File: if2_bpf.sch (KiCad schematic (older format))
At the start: 16 parts

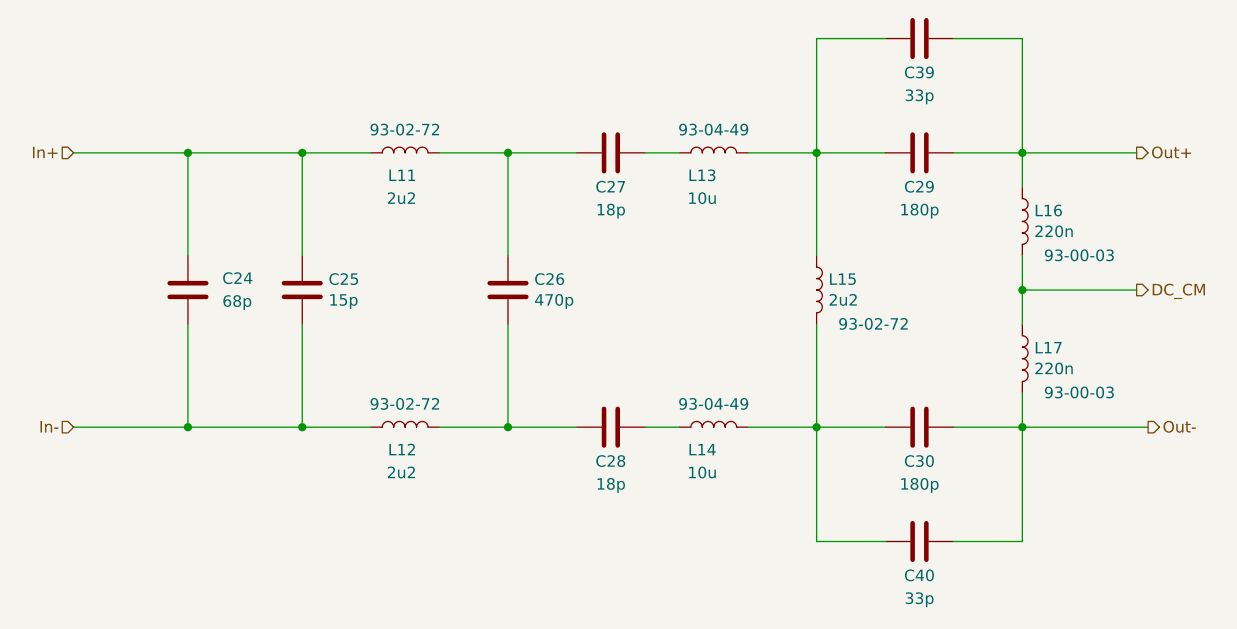
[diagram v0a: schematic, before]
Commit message: FPGA change and new project file
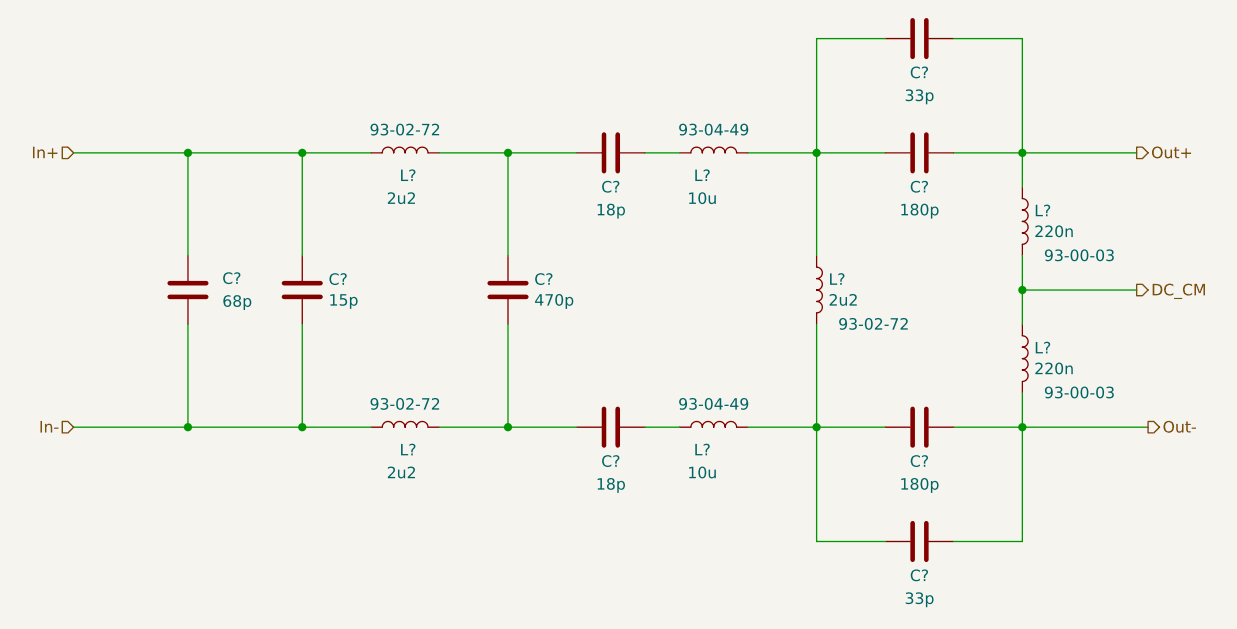
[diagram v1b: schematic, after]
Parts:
- renumbered C24 to C?, C25 to C?, C27 to C?, C29 to C?, C30 to C?, C28 to C?, C26 to C?, C39 to C?, C40 to C?, L13 to L?, L15 to L?, L16 to L?, L11 to L?, L12 to L?, L14 to L?, L17 to L?
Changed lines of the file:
@@
 $Descr A4 11693 8268
 encoding utf-8
-Sheet 5 7
+Sheet 5 12
 Title "9 MHz IF filter"
 Date "2021-01-15"
@@
 In-
 $Comp
-L Device:C C24
+L Device:C C?
 U 1 1 5FECCD6C
 P 4100 3950
-F 0 "C24" H 4250 4000 50  0000 L CNN
+F 0 "C?" H 4250 4000 50  0000 L CNN
 F 1 "68p" H 4250 3900 50  0000 L CNN
 F 2 "Capacitor_SMD:C_0805_2012Metric_Pad1.18x1.45mm_HandSolder" H 4138 3800 50  0001 C CNN
@@
 $EndComp
 $Comp
-L Device:C C25
+L Device:C C?
 U 1 1 5FECE707
 P 4600 3950
-F 0 "C25" H 4715 3996 50  0000 L CNN
+F 0 "C?" H 4715 3996 50  0000 L CNN
 F 1 "15p" H 4715 3905 50  0000 L CNN
 F 2 "Capacitor_SMD:C_0805_2012Metric_Pad1.18x1.45mm_HandSolder" H 4638 3800 50  0001 C CNN
@@
 $EndComp
 $Comp
-L Device:C C27
+L Device:C C?
 U 1 1 5FECF0CE
 P 5950 3350
-F 0 "C27" V 6100 3350 50  0000 C CNN
+F 0 "C?" V 6100 3350 50  0000 C CNN
 F 1 "18p" V 6200 3350 50  0000 C CNN
 F 2 "Capacitor_SMD:C_0805_2012Metric_Pad1.18x1.45mm_HandSolder" H 5988 3200 50  0001 C CNN
@@
 $EndComp
 $Comp
-L Device:L L13
+L Device:L L?
 U 1 1 5FECF5C4
 P 6400 3350
-F 0 "L13" V 6300 3400 50  0000 C CNN
+F 0 "L?" V 6300 3400 50  0000 C CNN
 F 1 "10u" V 6200 3400 50  0000 C CNN
 F 2 "Inductor_SMD:L_1210_3225Metric_Pad1.42x2.65mm_HandSolder" H 6400 3350 50  0001 C CNN
@@
 $EndComp
 $Comp
-L Device:L L15
+L Device:L L?
 U 1 1 5FED0166
 P 6850 3950
-F 0 "L15" H 6902 3996 50  0000 L CNN
+F 0 "L?" H 6902 3996 50  0000 L CNN
 F 1 "2u2" H 6902 3905 50  0000 L CNN
 F 2 "Inductor_SMD:L_0805_2012Metric_Pad1.15x1.40mm_HandSolder" H 6850 3950 50  0001 C CNN
@@
 $EndComp
 $Comp
-L Device:C C29
+L Device:C C?
 U 1 1 5FED1E6D
 P 7300 3350
-F 0 "C29" V 7450 3350 50  0000 C CNN
+F 0 "C?" V 7450 3350 50  0000 C CNN
 F 1 "180p" V 7550 3350 50  0000 C CNN
 F 2 "Capacitor_SMD:C_0805_2012Metric_Pad1.18x1.45mm_HandSolder" H 7338 3200 50  0001 C CNN
@@
 $EndComp
 $Comp
-L Device:L L16
+L Device:L L?
 U 1 1 5FED258A
 P 7750 3650
-F 0 "L16" H 7802 3696 50  0000 L CNN
+F 0 "L?" H 7802 3696 50  0000 L CNN
 F 1 "220n" H 7802 3605 50  0000 L CNN
 F 2 "Inductor_SMD:L_1210_3225Metric_Pad1.42x2.65mm_HandSolder" H 7750 3650 50  0001 C CNN
@@
 DC_CM
 $Comp
-L Device:C C30
+L Device:C C?
 U 1 1 5FED6CF7
 P 7300 4550
-F 0 "C30" V 7150 4550 50  0000 C CNN
+F 0 "C?" V 7150 4550 50  0000 C CNN
 F 1 "180p" V 7050 4550 50  0000 C CNN
 F 2 "Capacitor_SMD:C_0805_2012Metric_Pad1.18x1.45mm_HandSolder" H 7338 4400 50  0001 C CNN
@@
 $EndComp
 $Comp
-L Device:C C28
+L Device:C C?
 U 1 1 5FED7DBE
 P 5950 4550
-F 0 "C28" V 6100 4550 50  0000 C CNN
+F 0 "C?" V 6100 4550 50  0000 C CNN
 F 1 "18p" V 6200 4550 50  0000 C CNN
 F 2 "Capacitor_SMD:C_0805_2012Metric_Pad1.18x1.45mm_HandSolder" H 5988 4400 50  0001 C CNN
@@
 $EndComp
 $Comp
-L Device:C C26
+L Device:C C?
 U 1 1 5FEE51AD
 P 5500 3950
-F 0 "C26" H 5615 3996 50  0000 L CNN
+F 0 "C?" H 5615 3996 50  0000 L CNN
 F 1 "470p" H 5615 3905 50  0000 L CNN
 F 2 "Capacitor_SMD:C_0805_2012Metric_Pad1.18x1.45mm_HandSolder" H 5538 3800 50  0001 C CNN
@@
 $EndComp
 $Comp
-L Device:L L11
+L Device:L L?
 U 1 1 60028C2F
 P 5050 3350
-F 0 "L11" V 4950 3300 50  0000 L CNN
+F 0 "L?" V 4950 3300 50  0000 L CNN
 F 1 "2u2" V 4850 3300 50  0000 L CNN
 F 2 "Inductor_SMD:L_0805_2012Metric_Pad1.15x1.40mm_HandSolder" H 5050 3350 50  0001 C CNN
@@
 $EndComp
 $Comp
-L Device:L L12
+L Device:L L?
 U 1 1 6002A199
 P 5050 4550
-F 0 "L12" V 4950 4500 50  0000 L CNN
+F 0 "L?" V 4950 4500 50  0000 L CNN
 F 1 "2u2" V 4850 4500 50  0000 L CNN
 F 2 "Inductor_SMD:L_0805_2012Metric_Pad1.15x1.40mm_HandSolder" H 5050 4550 50  0001 C CNN
@@
 $EndComp
 $Comp
-L Device:L L14
+L Device:L L?
 U 1 1 6002AC30
 P 6400 4550
-F 0 "L14" V 6300 4600 50  0000 C CNN
+F 0 "L?" V 6300 4600 50  0000 C CNN
 F 1 "10u" V 6200 4600 50  0000 C CNN
 F 2 "Inductor_SMD:L_1210_3225Metric_Pad1.42x2.65mm_HandSolder" H 6400 4550 50  0001 C CNN
@@
 $EndComp
 $Comp
-L Device:L L17
+L Device:L L?
 U 1 1 6002B609
 P 7750 4250
-F 0 "L17" H 7802 4296 50  0000 L CNN
+F 0 "L?" H 7802 4296 50  0000 L CNN
 F 1 "220n" H 7802 4205 50  0000 L CNN
 F 2 "Inductor_SMD:L_1210_3225Metric_Pad1.42x2.65mm_HandSolder" H 7750 4250 50  0001 C CNN
@@
 Connection ~ 7750 4550
 $Comp
-L Device:C C39
+L Device:C C?
 U 1 1 6002CCED
 P 7300 2850
-F 0 "C39" V 7450 2850 50  0000 C CNN
+F 0 "C?" V 7450 2850 50  0000 C CNN
 F 1 "33p" V 7550 2850 50  0000 C CNN
 F 2 "Capacitor_SMD:C_0805_2012Metric_Pad1.18x1.45mm_HandSolder" H 7338 2700 50  0001 C CNN
@@
 $EndComp
 $Comp
-L Device:C C40
+L Device:C C?
 U 1 1 6002D1C8
 P 7300 5050
-F 0 "C40" V 7150 5050 50  0000 C CNN
+F 0 "C?" V 7150 5050 50  0000 C CNN
 F 1 "33p" V 7050 5050 50  0000 C CNN
 F 2 "Capacitor_SMD:C_0805_2012Metric_Pad1.18x1.45mm_HandSolder" H 7338 4900 50  0001 C CNN

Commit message: PCB is Done... Needs DRC check
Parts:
- gave numbers to parts that had none: 16
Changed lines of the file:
@@
 $Descr A4 11693 8268
 encoding utf-8
-Sheet 6 14
+Sheet 6 7
 Title "9 MHz IF filter"
 Date "2021-01-15"
@@
 In-
 $Comp
-L Device:C C?
+L Device:C C23
 U 1 1 5FECCD6C
 P 4100 3950
-F 0 "C?" H 4250 4000 50  0000 L CNN
+F 0 "C23" H 4250 4000 50  0000 L CNN
 F 1 "68p" H 4250 3900 50  0000 L CNN
 F 2 "Capacitor_SMD:C_0805_2012Metric_Pad1.18x1.45mm_HandSolder" H 4138 3800 50  0001 C CNN
@@
 $EndComp
 $Comp
-L Device:C C?
+L Device:C C24
 U 1 1 5FECE707
 P 4600 3950
-F 0 "C?" H 4715 3996 50  0000 L CNN
+F 0 "C24" H 4715 3996 50  0000 L CNN
 F 1 "15p" H 4715 3905 50  0000 L CNN
 F 2 "Capacitor_SMD:C_0805_2012Metric_Pad1.18x1.45mm_HandSolder" H 4638 3800 50  0001 C CNN
@@
 $EndComp
 $Comp
-L Device:C C?
+L Device:C C26
 U 1 1 5FECF0CE
 P 5950 3350
-F 0 "C?" V 6100 3350 50  0000 C CNN
+F 0 "C26" V 6100 3350 50  0000 C CNN
 F 1 "18p" V 6200 3350 50  0000 C CNN
 F 2 "Capacitor_SMD:C_0805_2012Metric_Pad1.18x1.45mm_HandSolder" H 5988 3200 50  0001 C CNN
@@
 $EndComp
 $Comp
-L Device:L L?
+L Device:L L12
 U 1 1 5FECF5C4
 P 6400 3350
-F 0 "L?" V 6300 3400 50  0000 C CNN
+F 0 "L12" V 6300 3400 50  0000 C CNN
 F 1 "10u" V 6200 3400 50  0000 C CNN
 F 2 "Inductor_SMD:L_1210_3225Metric_Pad1.42x2.65mm_HandSolder" H 6400 3350 50  0001 C CNN
@@
 $EndComp
 $Comp
-L Device:L L?
+L Device:L L14
 U 1 1 5FED0166
 P 6850 3950
-F 0 "L?" H 6902 3996 50  0000 L CNN
+F 0 "L14" H 6902 3996 50  0000 L CNN
 F 1 "2u2" H 6902 3905 50  0000 L CNN
 F 2 "Inductor_SMD:L_0805_2012Metric_Pad1.15x1.40mm_HandSolder" H 6850 3950 50  0001 C CNN
@@
 $EndComp
 $Comp
-L Device:C C?
+L Device:C C29
 U 1 1 5FED1E6D
 P 7300 3350
-F 0 "C?" V 7450 3350 50  0000 C CNN
+F 0 "C29" V 7450 3350 50  0000 C CNN
 F 1 "180p" V 7550 3350 50  0000 C CNN
 F 2 "Capacitor_SMD:C_0805_2012Metric_Pad1.18x1.45mm_HandSolder" H 7338 3200 50  0001 C CNN
@@
 $EndComp
 $Comp
-L Device:L L?
+L Device:L L15
 U 1 1 5FED258A
 P 7750 3650
-F 0 "L?" H 7802 3696 50  0000 L CNN
+F 0 "L15" H 7802 3696 50  0000 L CNN
 F 1 "220n" H 7802 3605 50  0000 L CNN
 F 2 "Inductor_SMD:L_1210_3225Metric_Pad1.42x2.65mm_HandSolder" H 7750 3650 50  0001 C CNN
@@
 DC_CM
 $Comp
-L Device:C C?
+L Device:C C30
 U 1 1 5FED6CF7
 P 7300 4550
-F 0 "C?" V 7150 4550 50  0000 C CNN
+F 0 "C30" V 7150 4550 50  0000 C CNN
 F 1 "180p" V 7050 4550 50  0000 C CNN
 F 2 "Capacitor_SMD:C_0805_2012Metric_Pad1.18x1.45mm_HandSolder" H 7338 4400 50  0001 C CNN
@@
 $EndComp
 $Comp
-L Device:C C?
+L Device:C C27
 U 1 1 5FED7DBE
 P 5950 4550
-F 0 "C?" V 6100 4550 50  0000 C CNN
+F 0 "C27" V 6100 4550 50  0000 C CNN
 F 1 "18p" V 6200 4550 50  0000 C CNN
 F 2 "Capacitor_SMD:C_0805_2012Metric_Pad1.18x1.45mm_HandSolder" H 5988 4400 50  0001 C CNN
@@
 $EndComp
 $Comp
-L Device:C C?
+L Device:C C25
 U 1 1 5FEE51AD
 P 5500 3950
-F 0 "C?" H 5615 3996 50  0000 L CNN
+F 0 "C25" H 5615 3996 50  0000 L CNN
 F 1 "470p" H 5615 3905 50  0000 L CNN
 F 2 "Capacitor_SMD:C_0805_2012Metric_Pad1.18x1.45mm_HandSolder" H 5538 3800 50  0001 C CNN
@@
 $EndComp
 $Comp
-L Device:L L?
+L Device:L L10
 U 1 1 60028C2F
 P 5050 3350
-F 0 "L?" V 4950 3300 50  0000 L CNN
+F 0 "L10" V 4950 3300 50  0000 L CNN
 F 1 "2u2" V 4850 3300 50  0000 L CNN
 F 2 "Inductor_SMD:L_0805_2012Metric_Pad1.15x1.40mm_HandSolder" H 5050 3350 50  0001 C CNN
@@
 $EndComp
 $Comp
-L Device:L L?
+L Device:L L11
 U 1 1 6002A199
 P 5050 4550
-F 0 "L?" V 4950 4500 50  0000 L CNN
+F 0 "L11" V 4950 4500 50  0000 L CNN
 F 1 "2u2" V 4850 4500 50  0000 L CNN
 F 2 "Inductor_SMD:L_0805_2012Metric_Pad1.15x1.40mm_HandSolder" H 5050 4550 50  0001 C CNN
@@
 $EndComp
 $Comp
-L Device:L L?
+L Device:L L13
 U 1 1 6002AC30
 P 6400 4550
-F 0 "L?" V 6300 4600 50  0000 C CNN
+F 0 "L13" V 6300 4600 50  0000 C CNN
 F 1 "10u" V 6200 4600 50  0000 C CNN
 F 2 "Inductor_SMD:L_1210_3225Metric_Pad1.42x2.65mm_HandSolder" H 6400 4550 50  0001 C CNN
@@
 $EndComp
 $Comp
-L Device:L L?
+L Device:L L16
 U 1 1 6002B609
 P 7750 4250
-F 0 "L?" H 7802 4296 50  0000 L CNN
+F 0 "L16" H 7802 4296 50  0000 L CNN
 F 1 "220n" H 7802 4205 50  0000 L CNN
 F 2 "Inductor_SMD:L_1210_3225Metric_Pad1.42x2.65mm_HandSolder" H 7750 4250 50  0001 C CNN
@@
 Connection ~ 7750 4550
 $Comp
-L Device:C C?
+L Device:C C28
 U 1 1 6002CCED
 P 7300 2850
-F 0 "C?" V 7450 2850 50  0000 C CNN
+F 0 "C28" V 7450 2850 50  0000 C CNN
 F 1 "33p" V 7550 2850 50  0000 C CNN
 F 2 "Capacitor_SMD:C_0805_2012Metric_Pad1.18x1.45mm_HandSolder" H 7338 2700 50  0001 C CNN
@@
 $EndComp
 $Comp
-L Device:C C?
+L Device:C C31
 U 1 1 6002D1C8
 P 7300 5050
-F 0 "C?" V 7150 5050 50  0000 C CNN
+F 0 "C31" V 7150 5050 50  0000 C CNN
 F 1 "33p" V 7050 5050 50  0000 C CNN
 F 2 "Capacitor_SMD:C_0805_2012Metric_Pad1.18x1.45mm_HandSolder" H 7338 4900 50  0001 C CNN
